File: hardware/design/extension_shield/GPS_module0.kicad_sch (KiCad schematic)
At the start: 1 part, among them J7 Conn_01x05_Socket

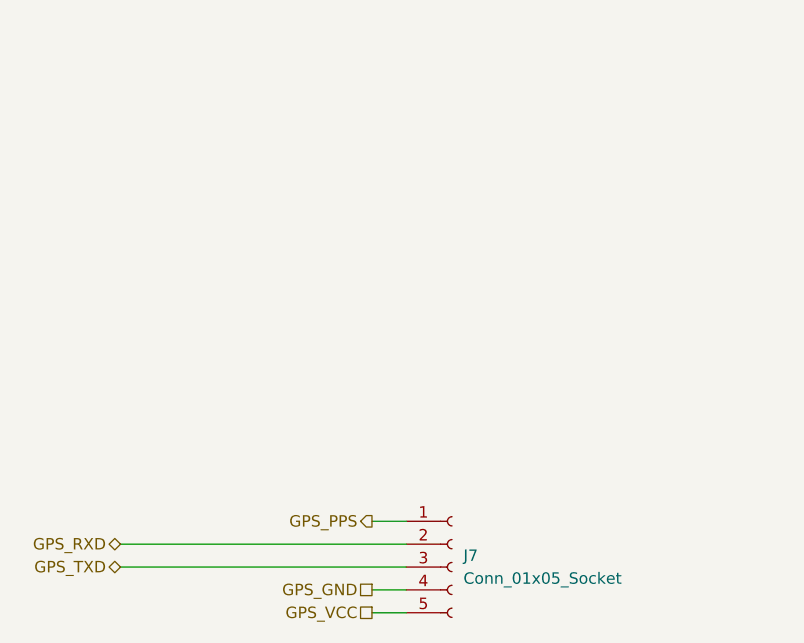
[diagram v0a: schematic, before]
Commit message: [HW/SHIELD] Adds Genereated PDF Schematic & Newer Version of Expansion Shield.
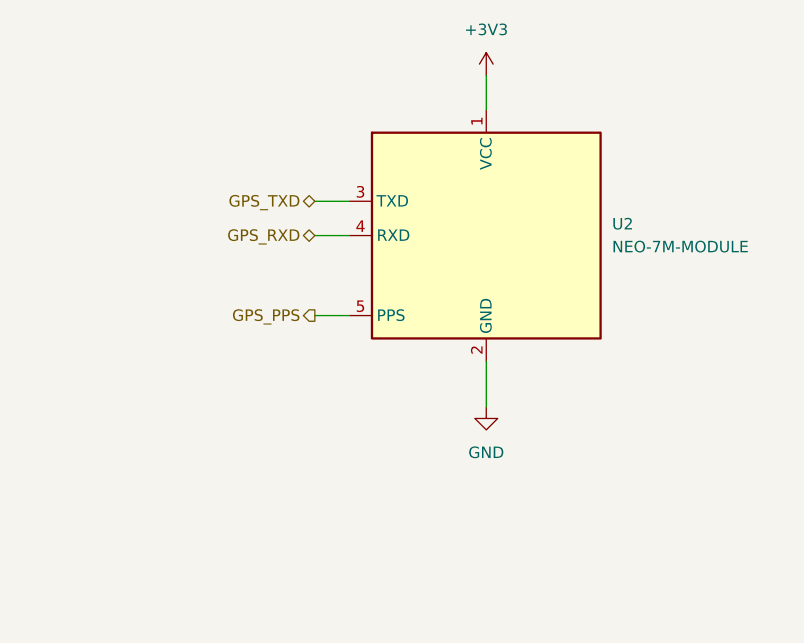
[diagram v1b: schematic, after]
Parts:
- removed J7: Conn_01x05_Socket, Connector_PinSocket_2.54mm:PinSocket_1x05_P2.54mm_Horizontal, symbol Connector:Conn_01x05_Socket
- added U2: NEO-7M-MODULE, Neo7M_Module_Lib:Neo-7M-Module, symbol Neo7M_Module_Lib:NEO-7M-MODULE
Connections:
- net GPS_PPS: now also U2.5 (PPS)
- net GPS_RXD: now also U2.4 (RXD)
- net GPS_TXD: now also U2.3 (TXD)
- new net +3V3: U2.1 (VCC)
- new net GND: U2.2 (GND)
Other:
- title: (none) -> Datalogger Expansion Shield
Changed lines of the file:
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@@
 	(generator_version "8.0")
 	(paper "A4")
-	(wire
-		(pts
-			(xy 158.75 129.54) (xy 190.5 129.54)
-		)
-		(stroke
-			(width 0)
-			(type default)
-		)
-	)
-	(wire
-		(pts
-			(xy 186.69 137.16) (xy 190.5 137.16)
-		)
-		(stroke
-			(width 0)
-			(type default)
-		)
-	)
-	(wire
-		(pts
-			(xy 186.69 134.62) (xy 190.5 134.62)
-		)
-		(stroke
-			(width 0)
-			(type default)
-		)
-	)
-	(wire
-		(pts
-			(xy 186.69 127) (xy 190.5 127)
-		)
-		(stroke
-			(width 0)
-			(type default)
-		)
-	)
-	(wire
-		(pts
-			(xy 158.75 132.08) (xy 190.5 132.08)
-		)
-		(stroke
-			(width 0)
-			(type default)
-		)
-	)
-	(hierarchical_label "GPS_GND"
-		(shape passive)
-		(at 186.69 134.62 180)
+	(title_block
+		(title "Datalogger Expansion Shield")
+		(date "2025-02-26")
+		(rev "1.2")
+	)
+	(wire
+		(pts
+			(xy 199.39 77.47) (xy 199.39 81.28)
+		)
+		(stroke
+			(width 0)
+			(type default)
+		)
+	)
+	(wire
+		(pts
+			(xy 180.34 95.25) (xy 184.15 95.25)
+		)
+		(stroke
+			(width 0)
+			(type default)
+		)
+	)
+	(wire
+		(pts
+			(xy 180.34 104.14) (xy 184.15 104.14)
+		)
+		(stroke
+			(width 0)
+			(type default)
+		)
+	)
+	(wire
+		(pts
+			(xy 180.34 91.44) (xy 184.15 91.44)
+		)
+		(stroke
+			(width 0)
+			(type default)
+		)
+	)
+	(wire
+		(pts
+			(xy 199.39 114.3) (xy 199.39 109.22)
+		)
+		(stroke
+			(width 0)
+			(type default)
+		)
+	)
+	(hierarchical_label "GPS_PPS"
+		(shape output)
+		(at 180.34 104.14 180)
 		(fields_autoplaced yes)
 		(effects
@@
 		)
 	)
-	(hierarchical_label "GPS_VCC"
-		(shape passive)
-		(at 186.69 137.16 180)
+	(hierarchical_label "GPS_RXD"
+		(shape bidirectional)
+		(at 180.34 95.25 180)
 		(fields_autoplaced yes)
 		(effects
@@
 	(hierarchical_label "GPS_TXD"
 		(shape bidirectional)
-		(at 158.75 132.08 180)
+		(at 180.34 91.44 180)
 		(fields_autoplaced yes)
 		(effects
@@
 		)
 	)
-	(hierarchical_label "GPS_PPS"
-		(shape output)
-		(at 186.69 127 180)
-		(fields_autoplaced yes)
-		(effects
-			(font
-				(size 1.27 1.27)
-			)
-			(justify right)
-		)
-	)
-	(hierarchical_label "GPS_RXD"
-		(shape bidirectional)
-		(at 158.75 129.54 180)
-		(fields_autoplaced yes)
-		(effects
-			(font
-				(size 1.27 1.27)
-			)
-			(justify right)
-		)
-	)
 	(symbol
-		(lib_id "Connector:Conn_01x05_Socket")
-		(at 195.58 132.08 0)
+		(lib_id "Neo7M_Module_Lib:NEO-7M-MODULE")
+		(at 199.39 106.68 0)
 		(unit 1)
 		(exclude_from_sim no)
@@
 		(dnp no)
 		(fields_autoplaced yes)
-		(property "Reference" "J7"
-			(at 196.85 130.8099 0)
+		(property "Reference" "U2"
+			(at 213.36 93.9799 0)
 			(effects
 				(font
@@
 			)
 		)
-		(property "Value" "Conn_01x05_Socket"
-			(at 196.85 133.3499 0)
+		(property "Value" "NEO-7M-MODULE"
+			(at 213.36 96.5199 0)
 			(effects
 				(font
@@
 			)
 		)
-		(property "Footprint" "Connector_PinSocket_2.54mm:PinSocket_1x05_P2.54mm_Horizontal"
-			(at 195.58 132.08 0)
-			(effects
-				(font
-					(size 1.27 1.27)
-				)
-				(hide yes)
-			)
-		)
-		(property "Datasheet" "~"
-			(at 195.58 132.08 0)
-			(effects
-				(font
-					(size 1.27 1.27)
-				)
-				(hide yes)
-			)
-		)
-		(property "Description" "Generic connector, single row, 01x05, script generated"
-			(at 195.58 132.08 0)
-			(effects
-				(font
-					(size 1.27 1.27)
-				)
-				(hide yes)
-			)
+		(property "Footprint" "Neo7M_Module_Lib:Neo-7M-Module"
+			(at 209.55 130.81 0)
+			(effects
+				(font
+					(size 1.27 1.27)
+				)
+				(hide yes)
+			)
+		)
+		(property "Datasheet" "https://www.mouser.co.uk/datasheet/2/1025/NEO_7_DataSheet__UBX_13003830_-2010064.pdf"
+			(at 199.39 106.68 0)
+			(effects
+				(font
+					(size 1.27 1.27)
+				)
+				(hide yes)
+			)
+		)
+		(property "Description" "GPS Module (Assembled miniBoard) Neo-7M-Module (https://dratek.cz/docs/produkty/0/474/1502177743.pdf)"
+			(at 199.39 106.68 0)
+			(effects
+				(font
+					(size 1.27 1.27)
+				)
+				(hide yes)
+			)
+		)
+		(pin "2"
+		)
+		(pin "5"
+		)
+		(pin "3"
 		)
 		(pin "4"
 		)
-		(pin "5"
-		)
 		(pin "1"
-		)
-		(pin "3"
-		)
-		(pin "2"
 		)
 		(instances
 			(project ""
 				(path "/eb423e93-ba35-4986-b1f5-42479ae2bfa7/e26a225d-238a-4cd1-9ea6-6c066c5d44e8"
-					(reference "J7")
+					(reference "U2")
 					(unit 1)
 				)
+			)
+		)
+	)
+	(symbol
+		(lib_id "power:GND")
+		(at 199.39 114.3 0)
+		(unit 1)
+		(exclude_from_sim no)
+		(in_bom yes)
+		(on_board yes)
+		(dnp no)
+		(fields_autoplaced yes)
+		(property "Reference" "#PWR026"
+			(at 199.39 120.65 0)
+			(effects
+				(font
+					(size 1.27 1.27)
+				)
+				(hide yes)
+			)
+		)
+		(property "Value" "GND"
+			(at 199.39 119.38 0)
+			(effects
+				(font
+					(size 1.27 1.27)
+				)
+			)
+		)
+		(property "Footprint" ""
+			(at 199.39 114.3 0)
+			(effects
+				(font
+					(size 1.27 1.27)
+				)
+				(hide yes)
+			)
+		)
+		(property "Datasheet" ""
+			(at 199.39 114.3 0)
+			(effects
+				(font
+					(size 1.27 1.27)
+				)
+				(hide yes)
+			)
+		)
+		(property "Description" "Power symbol creates a global label with name \"GND\" , ground"
+			(at 199.39 114.3 0)
+			(effects
+				(font
+					(size 1.27 1.27)
+				)
+				(hide yes)
+			)
+		)
+		(pin "1"
+		)
+		(instances
+			(project "extension_shield"
+				(path "/eb423e93-ba35-4986-b1f5-42479ae2bfa7/e26a225d-238a-4cd1-9ea6-6c066c5d44e8"
+					(reference "#PWR026")
+					(unit 1)
+				)
+			)
+		)
+	)
+	(symbol
+		(lib_id "power:+3V3")
+		(at 199.39 77.47 0)
+		(unit 1)
+		(exclude_from_sim no)
+		(in_bom yes)
+		(on_board yes)
+		(dnp no)
+		(fields_autoplaced yes)
+		(property "Reference" "#PWR023"
+			(at 199.39 81.28 0)
+			(effects
+				(font
+					(size 1.27 1.27)
+				)
+				(hide yes)
+			)
+		)
+		(property "Value" "+3V3"
+			(at 199.39 72.39 0)
+			(effects
+				(font
+					(size 1.27 1.27)
+				)
+			)
+		)
+		(property "Footprint" ""
+			(at 199.39 77.47 0)
+			(effects
+				(font
+					(size 1.27 1.27)
+				)
+				(hide yes)
+			)
+		)
+		(property "Datasheet" ""
+			(at 199.39 77.47 0)
+			(effects
+				(font
+					(size 1.27 1.27)
+				)
+				(hide yes)
+			)
+		)
+		(property "Description" "Power symbol creates a global label with name \"+3V3\""
+			(at 199.39 77.47 0)
+			(effects
+				(font
+					(size 1.27 1.27)
+				)
+				(hide yes)
+			)
+		)
+		(pin "1"
+		)
+		(instances
+			(project "extension_shield"
+				(path "/eb423e93-ba35-4986-b1f5-42479ae2bfa7/e26a225d-238a-4cd1-9ea6-6c066c5d44e8"
+					(reference "#PWR023")
+					(unit 1)
+				)
